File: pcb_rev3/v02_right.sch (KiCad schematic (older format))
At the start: 72 parts, among them J1 MJ-4PP-9, SW1 SW_Push, U1 ProMicro

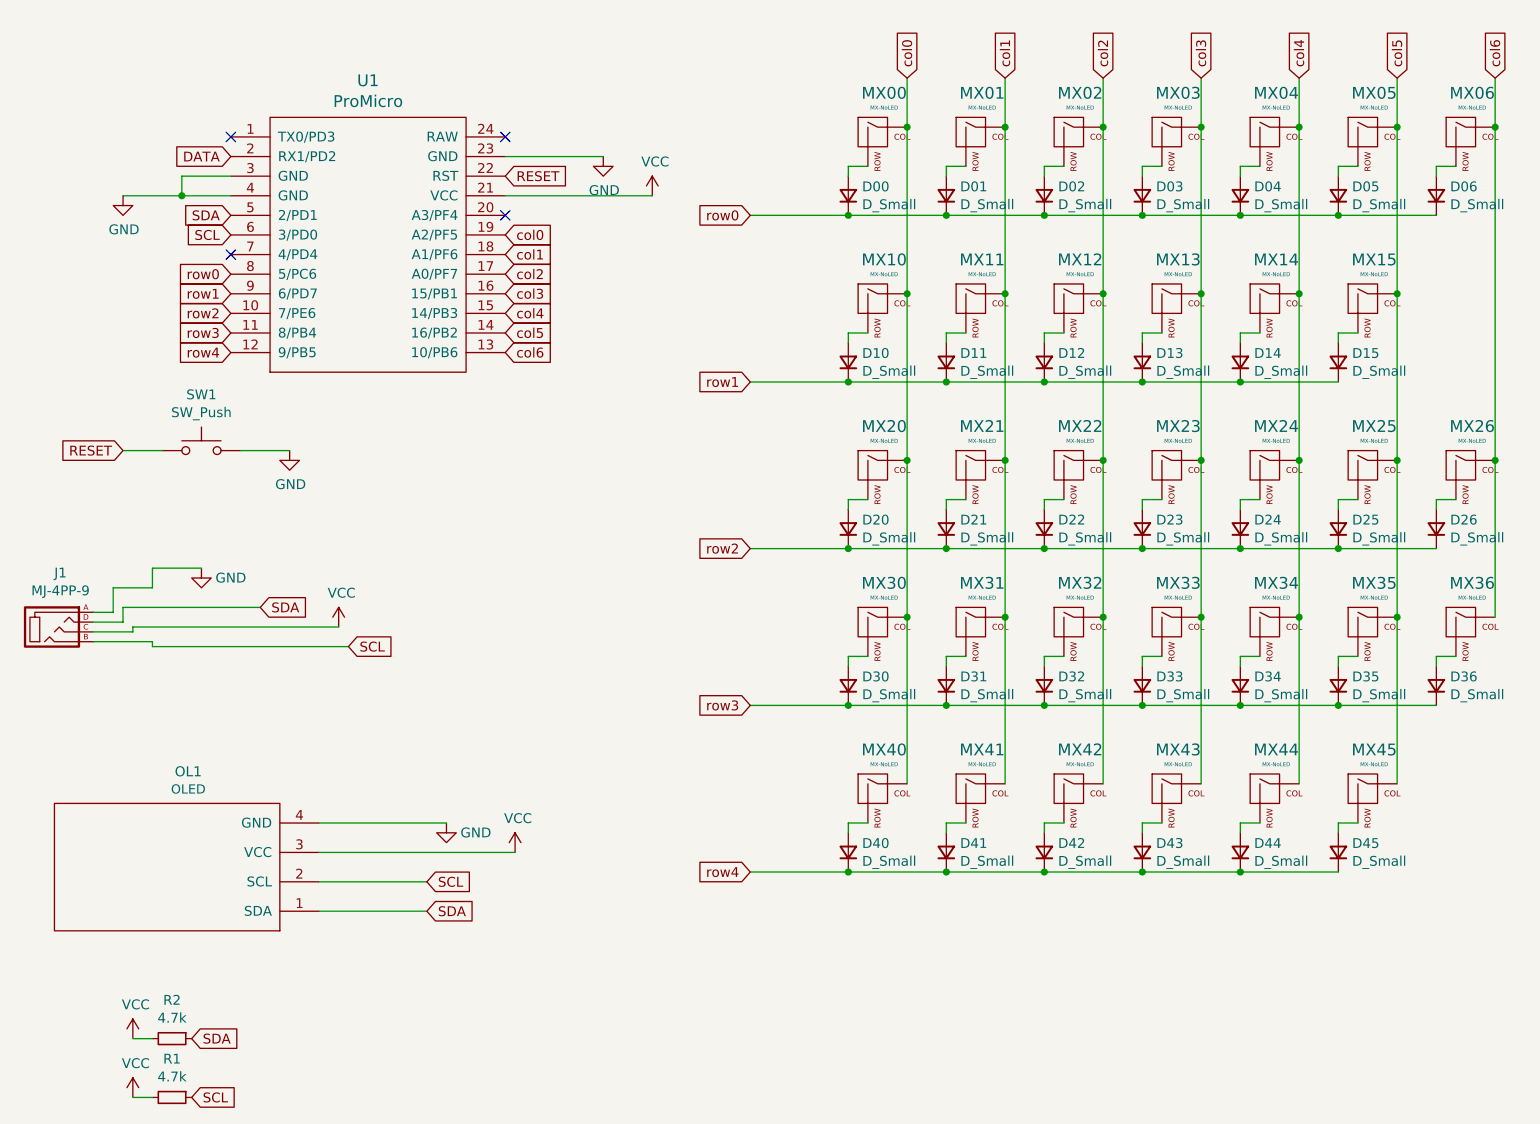
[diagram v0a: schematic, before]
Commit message: Started edits for right side for v0.3; added holes for OLED cover, fixed TRRS and reset switch footprints
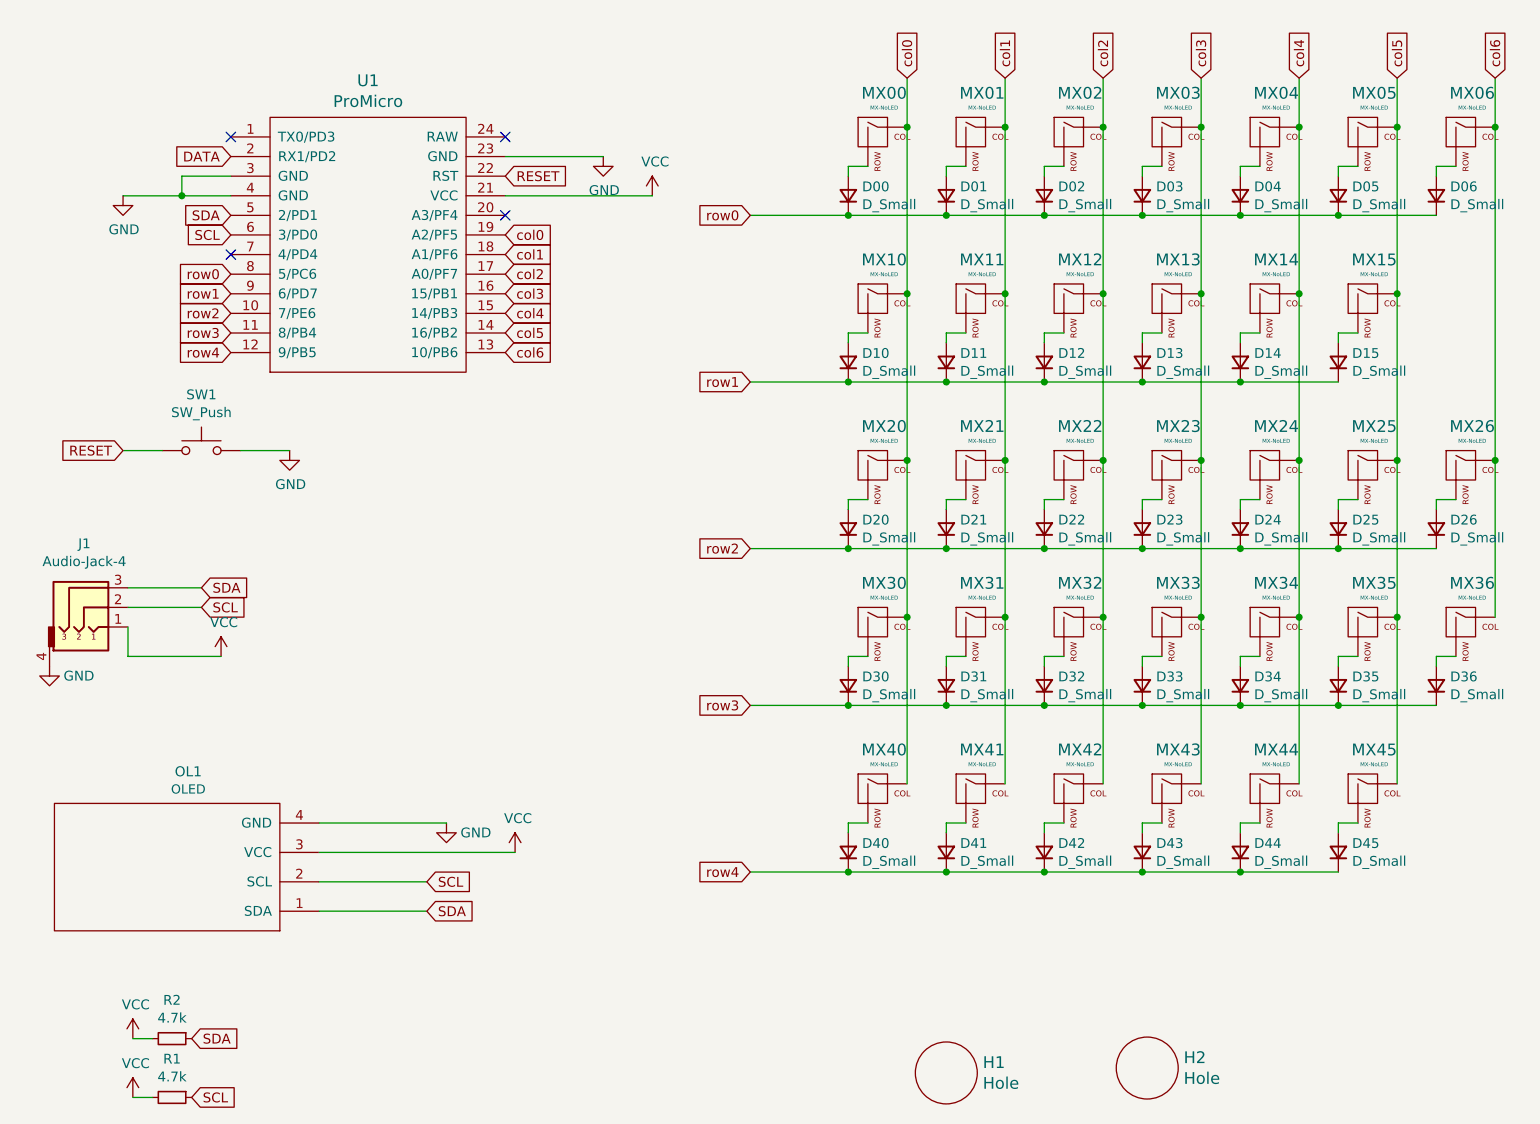
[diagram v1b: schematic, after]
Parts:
- removed J1: MJ-4PP-9, kbd:MJ-4PP-9_1side, symbol kbd:MJ-4PP-9
- added H1, H2: Hole, Lily58-footprint:HOLE_M2, symbol keebio:Hole
- added J1: Audio-Jack-4, Keebio-Parts:TRRS-PJ-320A, symbol redox_rev1-cache:Audio-Jack-4
- SW1: footprint kbd:ResetSW_4P -> Keebio-Parts:SW_Tactile_SPST_Angled_MJTP1117
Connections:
- net GND: now also J1.4
- net SCL: now also J1.2
- net SDA: now also J1.3
- net VCC: now also J1.1
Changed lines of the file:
@@
 F 0 "SW1" H 1500 2985 50  0000 C CNN
 F 1 "SW_Push" H 1500 2894 50  0000 C CNN
-F 2 "kbd:ResetSW_4P" H 1500 2900 50  0001 C CNN
+F 2 "Keebio-Parts:SW_Tactile_SPST_Angled_MJTP1117" H 1500 2900 50  0001 C CNN
 F 3 "~" H 1500 2900 50  0001 C CNN
 	1    1500 2700
@@
 L power:VCC #PWR0105
 U 1 1 60C8554A
-P 2200 3600
-F 0 "#PWR0105" H 2200 3450 50  0001 C CNN
-F 1 "VCC" H 2215 3773 50  0000 C CNN
-F 2 "" H 2200 3600 50  0001 C CNN
-F 3 "" H 2200 3600 50  0001 C CNN
-	1    2200 3600
+P 1600 3750
+F 0 "#PWR0105" H 1600 3600 50  0001 C CNN
+F 1 "VCC" H 1615 3923 50  0000 C CNN
+F 2 "" H 1600 3750 50  0001 C CNN
+F 3 "" H 1600 3750 50  0001 C CNN
+	1    1600 3750
 	1    0    0    -1
 $EndComp
@@
 L power:GND #PWR0106
 U 1 1 60C87D93
-P 1500 3300
-F 0 "#PWR0106" H 1500 3050 50  0001 C CNN
-F 1 "GND" H 1650 3250 50  0000 C CNN
-F 2 "" H 1500 3300 50  0001 C CNN
-F 3 "" H 1500 3300 50  0001 C CNN
-	1    1500 3300
-	1    0    0    -1
-$EndComp
-Wire Wire Line
-	1250 3400 1250 3300
-Wire Wire Line
-	1250 3300 1500 3300
+P 725 3800
+F 0 "#PWR0106" H 725 3550 50  0001 C CNN
+F 1 "GND" H 875 3750 50  0000 C CNN
+F 2 "" H 725 3800 50  0001 C CNN
+F 3 "" H 725 3800 50  0001 C CNN
+	1    725  3800
+	1    0    0    -1
+$EndComp
 $Comp
 L power:VCC #PWR0109
@@
 Text GLabel 2650 5050 2    50   Input ~ 0
 SDA
-$Comp
-L kbd:MJ-4PP-9 J1
-U 1 1 60CF63A6
-P 750 3600
-F 0 "J1" H 781 3876 50  0000 C CNN
-F 1 "MJ-4PP-9" H 781 3785 50  0000 C CNN
-F 2 "kbd:MJ-4PP-9_1side" H 1025 3775 50  0001 C CNN
-F 3 "~" H 1025 3775 50  0001 C CNN
-	1    750  3600
-	1    0    0    -1
-$EndComp
-Wire Wire Line
-	950  3525 1050 3525
-Wire Wire Line
-	1050 3525 1050 3400
-Wire Wire Line
-	1050 3400 1250 3400
-Wire Wire Line
-	950  3575 1100 3575
-Wire Wire Line
-	1100 3575 1100 3500
-Wire Wire Line
-	1100 3500 1800 3500
-Wire Wire Line
-	950  3625 1150 3625
-Wire Wire Line
-	1150 3625 1150 3600
-Wire Wire Line
-	1150 3600 2200 3600
-Wire Wire Line
-	950  3675 1250 3675
-Wire Wire Line
-	1250 3675 1250 3700
 Wire Wire Line
 	2100 4600 2750 4600
@@
 Wire Wire Line
 	2100 5050 2650 5050
-Wire Wire Line
-	1250 3700 2250 3700
-Text GLabel 2250 3700 2    50   Input ~ 0
+Text GLabel 1500 3500 2    50   Input ~ 0
 SCL
-Text GLabel 1800 3500 2    50   Input ~ 0
+Text GLabel 1500 3400 2    50   Input ~ 0
 SDA
+$Comp
+L keebio:Hole H1
+U 1 1 60F4BED8
+P 5300 5875
+F 0 "H1" H 5486 5928 60  0000 L CNN
+F 1 "Hole" H 5486 5822 60  0000 L CNN
+F 2 "Lily58-footprint:HOLE_M2" H 5300 5875 60  0001 C CNN
+F 3 "" H 5300 5875 60  0001 C CNN
+	1    5300 5875
+	1    0    0    -1
+$EndComp
+$Comp
+L keebio:Hole H2
+U 1 1 60F4D227
+P 6325 5850
+F 0 "H2" H 6511 5903 60  0000 L CNN
+F 1 "Hole" H 6511 5797 60  0000 L CNN
+F 2 "Lily58-footprint:HOLE_M2" H 6325 5850 60  0001 C CNN
+F 3 "" H 6325 5850 60  0001 C CNN
+	1    6325 5850
+	1    0    0    -1
+$EndComp
+$Comp
+L redox_rev1-cache:Audio-Jack-4 J1
+U 1 1 60F64E7C
+P 925 3400
+F 0 "J1" H 903 3625 50  0000 C CNN
+F 1 "Audio-Jack-4" H 903 3534 50  0000 C CNN
+F 2 "Keebio-Parts:TRRS-PJ-320A" H 1175 3500 50  0001 C CNN
+F 3 "" H 1175 3500 50  0001 C CNN
+	1    925  3400
+	1    0    0    -1
+$EndComp
+Wire Wire Line
+	1125 3400 1500 3400
+Wire Wire Line
+	1125 3500 1500 3500
+Wire Wire Line
+	1125 3600 1125 3750
+Wire Wire Line
+	1125 3750 1600 3750
 $EndSCHEMATC
